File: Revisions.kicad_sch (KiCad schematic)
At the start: 0 parts

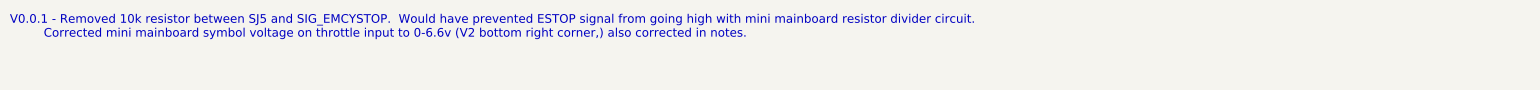
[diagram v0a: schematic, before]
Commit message: V0.0.3 update
Corrected L2 inductor to one properly sized.  From 0805 to a Sunlord 4030 / 4.0mmX4.0mm inductor.
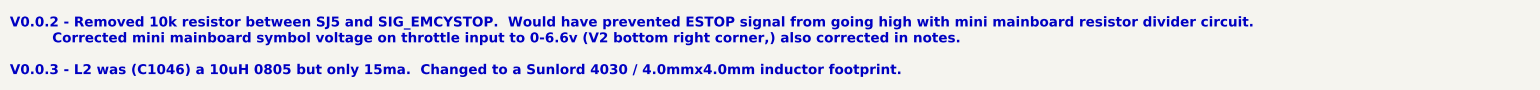
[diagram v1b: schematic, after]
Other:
- note added: "V0.0.2 - Removed 10k resistor between SJ5 and SIG_EMCYSTOP. Would have prevented ESTOP signal from going high with mini mainboard resistor divider circuit. Corrected mini mainboard symbol voltage on throttle input to 0-6.6v (V2 bottom right corner,) also corrected in notes. V0.0.3 - L2 was (C1046) a 10uH 0805 but only 15ma. Changed to a Sunlord 4030 / 4.0mmx4.0mm inductor footprint."
- note removed: "V0.0.1 - Removed 10k resistor between SJ5 and SIG_EMCYSTOP. Would have prevented ESTOP signal from going high with mini mainboard resistor divider circuit. Corrected mini mainboard symbol voltage on throttle input to 0-6.6v (V2 bottom right corner,) also corrected in notes."
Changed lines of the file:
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@@
 (kicad_sch (version 20211123) (generator eeschema)
   (paper "A4")
-  (text "V0.0.1 - Removed 10k resistor between SJ5 and SIG_EMCYSTOP.  Would have prevented ESTOP signal from going high with mini mainboard resistor divider circuit. \n         Corrected mini mainboard symbol voltage on throttle input to 0-6.6v (V2 bottom right corner,) also corrected in notes."
-    (at 15.24 19.05 0)
-    (effects (font (size 1.75 1.75)) (justify left bottom))
+  (title_block
+    (rev "V0.0.3")
+  )
+  (text "V0.0.2 - Removed 10k resistor between SJ5 and SIG_EMCYSTOP.  Would have prevented ESTOP signal from going high with mini mainboard resistor divider circuit. \n         Corrected mini mainboard symbol voltage on throttle input to 0-6.6v (V2 bottom right corner,) also corrected in notes.\n\nV0.0.3 - L2 was (C1046) a 10uH 0805 but only 15ma.  Changed to a Sunlord 4030 / 4.0mmx4.0mm inductor footprint."
+    (at 15.24 26.67 0)
+    (effects (font (size 2 2) (thickness 0.4) bold) (justify left bottom))
   )
 )
